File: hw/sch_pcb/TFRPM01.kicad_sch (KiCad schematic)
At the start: 28 parts, among them J1 HEADER_1x03, J2 SM04B-GHS-TB, J3 SM04B-GHS-TB, M2 M3, U1 PCF8583, U2 SN74LVC1G14-Q1, U3 MIC5504-3.3YM5

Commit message: Exclude Fiducial + SolderJumper_3_Bridged12 + M3 from BOM.
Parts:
- FID1, FID2, FID3, JP1, JP2, M2: now left out of the parts list
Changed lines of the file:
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@@
   )
   (symbol (lib_id "MLAB_MECHANICAL:HOLE") (at 265.43 21.59 90) (unit 1)
-    (in_bom yes) (on_board yes)
+    (in_bom no) (on_board yes)
     (property "Reference" "M2" (id 0) (at 265.43 24.13 90)
       (effects (font (size 1.524 1.524)))
@@
   )
   (symbol (lib_name "SolderJumper_3_Bridged12_1") (lib_id "Jumper:SolderJumper_3_Bridged12") (at 143.51 45.72 0) (unit 1)
-    (in_bom yes) (on_board yes)
+    (in_bom no) (on_board yes)
     (property "Reference" "JP2" (id 0) (at 143.51 43.1608 0))
     (property "Value" "SolderJumper_3_Bridged12" (id 1) (at 143.51 42.92 0)
@@
   )
   (symbol (lib_id "Mechanical:Fiducial") (at 216.535 22.225 0) (unit 1)
-    (in_bom yes) (on_board yes) (fields_autoplaced)
+    (in_bom no) (on_board yes) (fields_autoplaced)
     (property "Reference" "FID1" (id 0) (at 218.694 21.3165 0)
       (effects (font (size 1.27 1.27)) (justify left))
@@
   )
   (symbol (lib_id "Mechanical:Fiducial") (at 228.6 22.225 0) (unit 1)
-    (in_bom yes) (on_board yes) (fields_autoplaced)
+    (in_bom no) (on_board yes) (fields_autoplaced)
     (property "Reference" "FID2" (id 0) (at 230.759 21.3165 0)
       (effects (font (size 1.27 1.27)) (justify left))
@@
   )
   (symbol (lib_id "Jumper:SolderJumper_3_Bridged12") (at 100.33 107.95 0) (unit 1)
-    (in_bom yes) (on_board yes)
+    (in_bom no) (on_board yes)
     (property "Reference" "JP1" (id 0) (at 100.33 105.3908 0))
     (property "Value" "SolderJumper_3_Bridged12" (id 1) (at 100.33 105.15 0)
@@
   )
   (symbol (lib_id "Mechanical:Fiducial") (at 241.3 22.225 0) (unit 1)
-    (in_bom yes) (on_board yes) (fields_autoplaced)
+    (in_bom no) (on_board yes) (fields_autoplaced)
     (property "Reference" "FID3" (id 0) (at 243.459 21.3165 0)
       (effects (font (size 1.27 1.27)) (justify left))

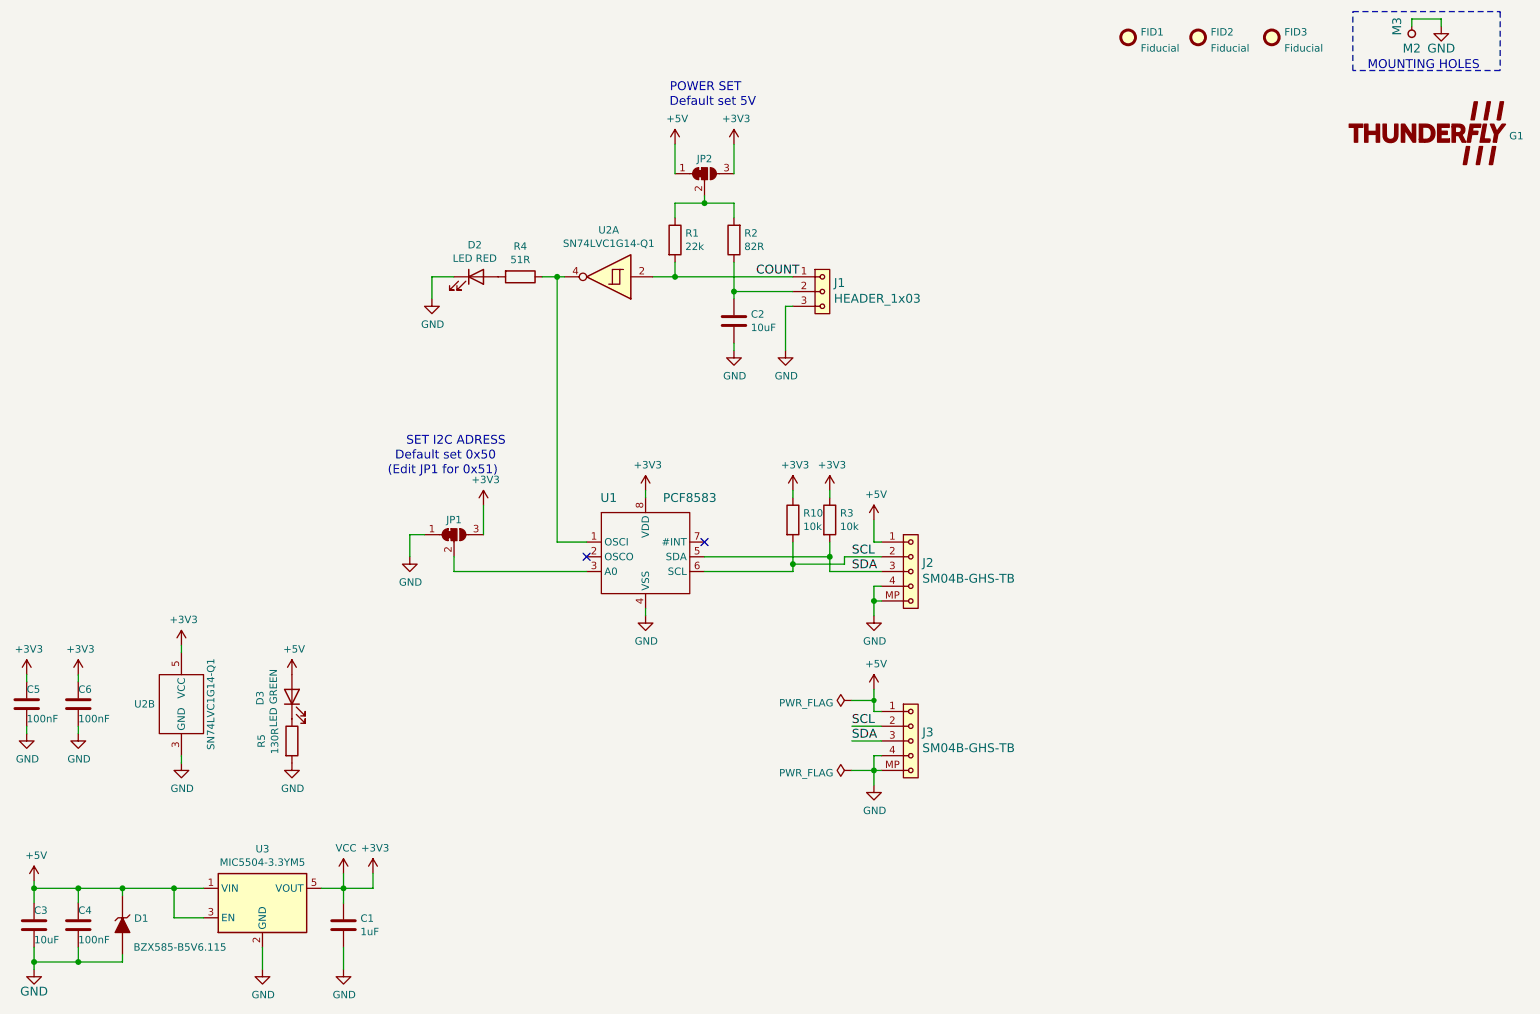
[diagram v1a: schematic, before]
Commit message: Update part number marking.
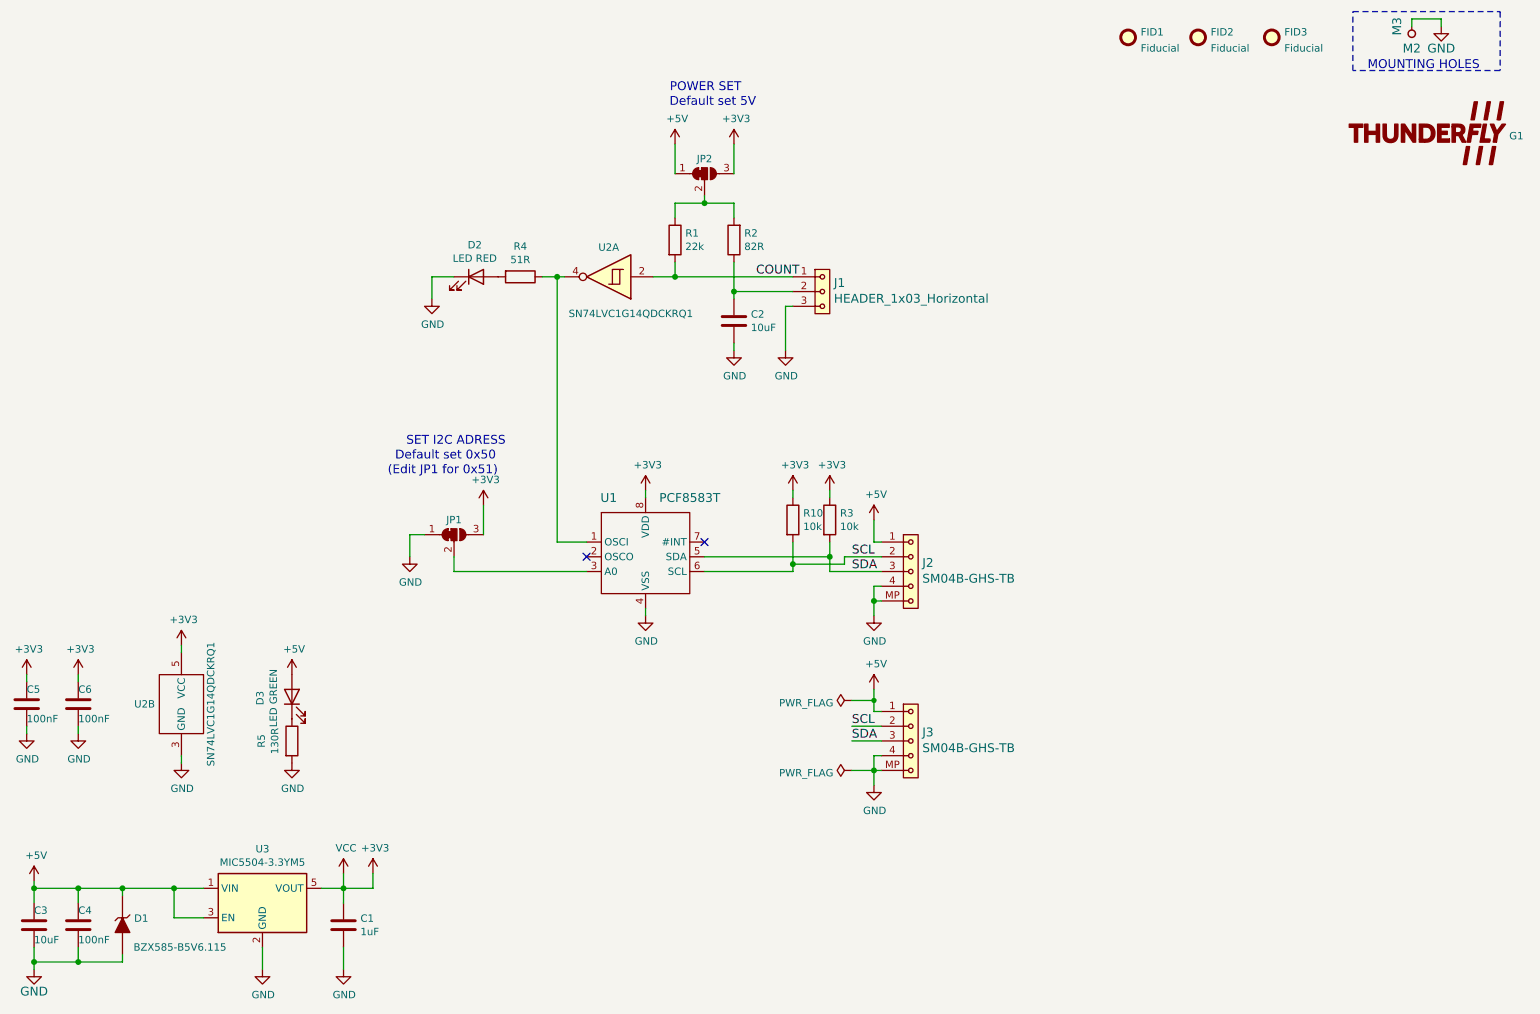
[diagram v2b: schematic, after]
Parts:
- J1: value HEADER_1x03 -> HEADER_1x03_Horizontal
- U1: value PCF8583 -> PCF8583T
- U2: value SN74LVC1G14-Q1 -> SN74LVC1G14QDCKRQ1
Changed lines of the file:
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@@
       (effects (font (size 1.524 1.524)))
     )
-    (property "Value" "PCF8583" (id 1) (at 140.97 101.6 0)
+    (property "Value" "PCF8583T" (id 1) (at 140.97 101.6 0)
       (effects (font (size 1.524 1.524)))
     )
@@
   (symbol (lib_id "MLAB_IO:74AHC1G14GV") (at 127 63.5 180) (unit 1)
     (in_bom yes) (on_board yes)
-    (property "Reference" "U2" (id 0) (at 127 55.4482 0))
-    (property "Value" "SN74LVC1G14-Q1" (id 1) (at 127 57.76 0))
+    (property "Reference" "U2" (id 0) (at 127 58.42 0))
+    (property "Value" "SN74LVC1G14QDCKRQ1" (id 1) (at 130.81 69.85 0))
     (property "Footprint" "Package_TO_SOT_SMD:SOT-353_SC-70-5" (id 2) (at 127 63.5 0)
       (effects (font (size 1.27 1.27)) hide)
@@
       (effects (font (size 1.524 1.524)) (justify left))
     )
-    (property "Value" "HEADER_1x03" (id 1) (at 165.8112 67.2592 0)
+    (property "Value" "HEADER_1x03_Horizontal" (id 1) (at 165.8112 67.2592 0)
       (effects (font (size 1.524 1.524)) (justify left))
     )
@@
     (in_bom yes) (on_board yes)
     (property "Reference" "U2" (id 0) (at 46.99 137.16 0))
-    (property "Value" "SN74LVC1G14-Q1" (id 1) (at 58.42 137.16 90))
+    (property "Value" "SN74LVC1G14QDCKRQ1" (id 1) (at 58.42 137.16 90))
     (property "Footprint" "Package_TO_SOT_SMD:SOT-353_SC-70-5" (id 2) (at 53.34 137.16 0)
       (effects (font (size 1.27 1.27)) hide)
@@
     )
     (path "/00000000-0000-0000-0000-00005de84efb"
-      (reference "J1") (unit 1) (value "HEADER_1x03") (footprint "Connector_PinHeader_2.54mm:PinHeader_1x03_P2.54mm_Horizontal")
+      (reference "J1") (unit 1) (value "HEADER_1x03_Horizontal") (footprint "Connector_PinHeader_2.54mm:PinHeader_1x03_P2.54mm_Horizontal")
     )
     (path "/00000000-0000-0000-0000-00005deb9c07"
@@
     )
     (path "/00000000-0000-0000-0000-000059ff55ba"
-      (reference "U1") (unit 1) (value "PCF8583") (footprint "Mlab_IO:SOT176-1")
+      (reference "U1") (unit 1) (value "PCF8583T") (footprint "Mlab_IO:SOT176-1")
     )
     (path "/00000000-0000-0000-0000-00005b1b4dea"
-      (reference "U2") (unit 1) (value "SN74LVC1G14-Q1") (footprint "Package_TO_SOT_SMD:SOT-353_SC-70-5")
+      (reference "U2") (unit 1) (value "SN74LVC1G14QDCKRQ1") (footprint "Package_TO_SOT_SMD:SOT-353_SC-70-5")
     )
     (path "/00000000-0000-0000-0000-00005ded0588"
-      (reference "U2") (unit 2) (value "SN74LVC1G14-Q1") (footprint "Package_TO_SOT_SMD:SOT-353_SC-70-5")
+      (reference "U2") (unit 2) (value "SN74LVC1G14QDCKRQ1") (footprint "Package_TO_SOT_SMD:SOT-353_SC-70-5")
     )
     (path "/00000000-0000-0000-0000-00005de928cf"
